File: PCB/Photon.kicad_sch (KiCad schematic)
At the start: 45 parts, among them J1 USB_C_Receptacle_USB2.0_14P, J2 Conn_01x05_Socket, Q1 IRLML6402, Q2 IRLML6402, SW1 TS-1088-AR02016, U1 PY32F002AL15S6TU, U2 TP4056, U3 RT8059GJ5, U4 BCR421UW6-7, U5 DW01A, U6 FS8205A, U7 BCR421UW6-7

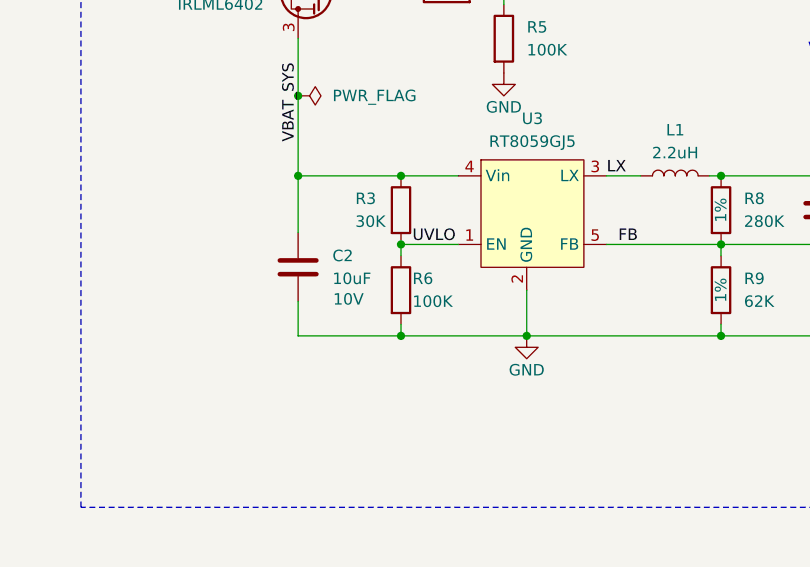
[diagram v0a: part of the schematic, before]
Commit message: updated debug header and changed resistors for UVLO
Applied teardrop to all vias. some were missing. Thickened trace from neg battery terminal. Updated gerbers
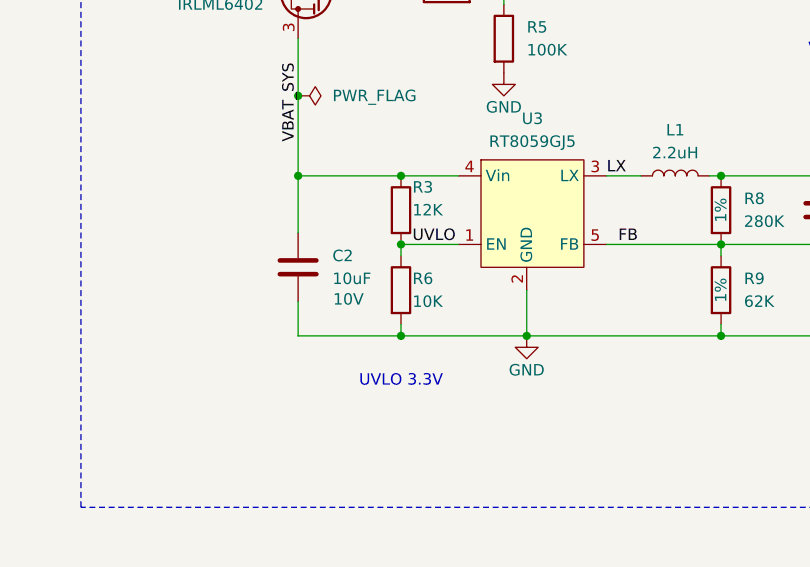
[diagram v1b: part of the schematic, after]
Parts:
- R3: value 30K -> 12K
- R6: value 100K -> 10K
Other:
- note added: "UVLO 3.3V"
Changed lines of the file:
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@@
 		)
 	)
+	(text "UVLO 3.3V\n"
+		(exclude_from_sim no)
+		(at 165.1 222.25 0)
+		(effects
+			(font
+				(size 1.27 1.27)
+			)
+		)
+	)
 	(text "If usb (5V) present \n-> disable buck"
 		(exclude_from_sim no)
@@
 			)
 		)
-		(property "Value" "100K"
+		(property "Value" "10K"
 			(at 166.37 213.36 0)
 			(effects
@@
 		(dnp no)
 		(property "Reference" "R3"
-			(at 160.02 201.93 0)
+			(at 166.37 200.66 0)
 			(effects
 				(font
@@
 			)
 		)
-		(property "Value" "30K"
-			(at 160.02 204.47 0)
+		(property "Value" "12K"
+			(at 166.37 203.2 0)
 			(effects
 				(font

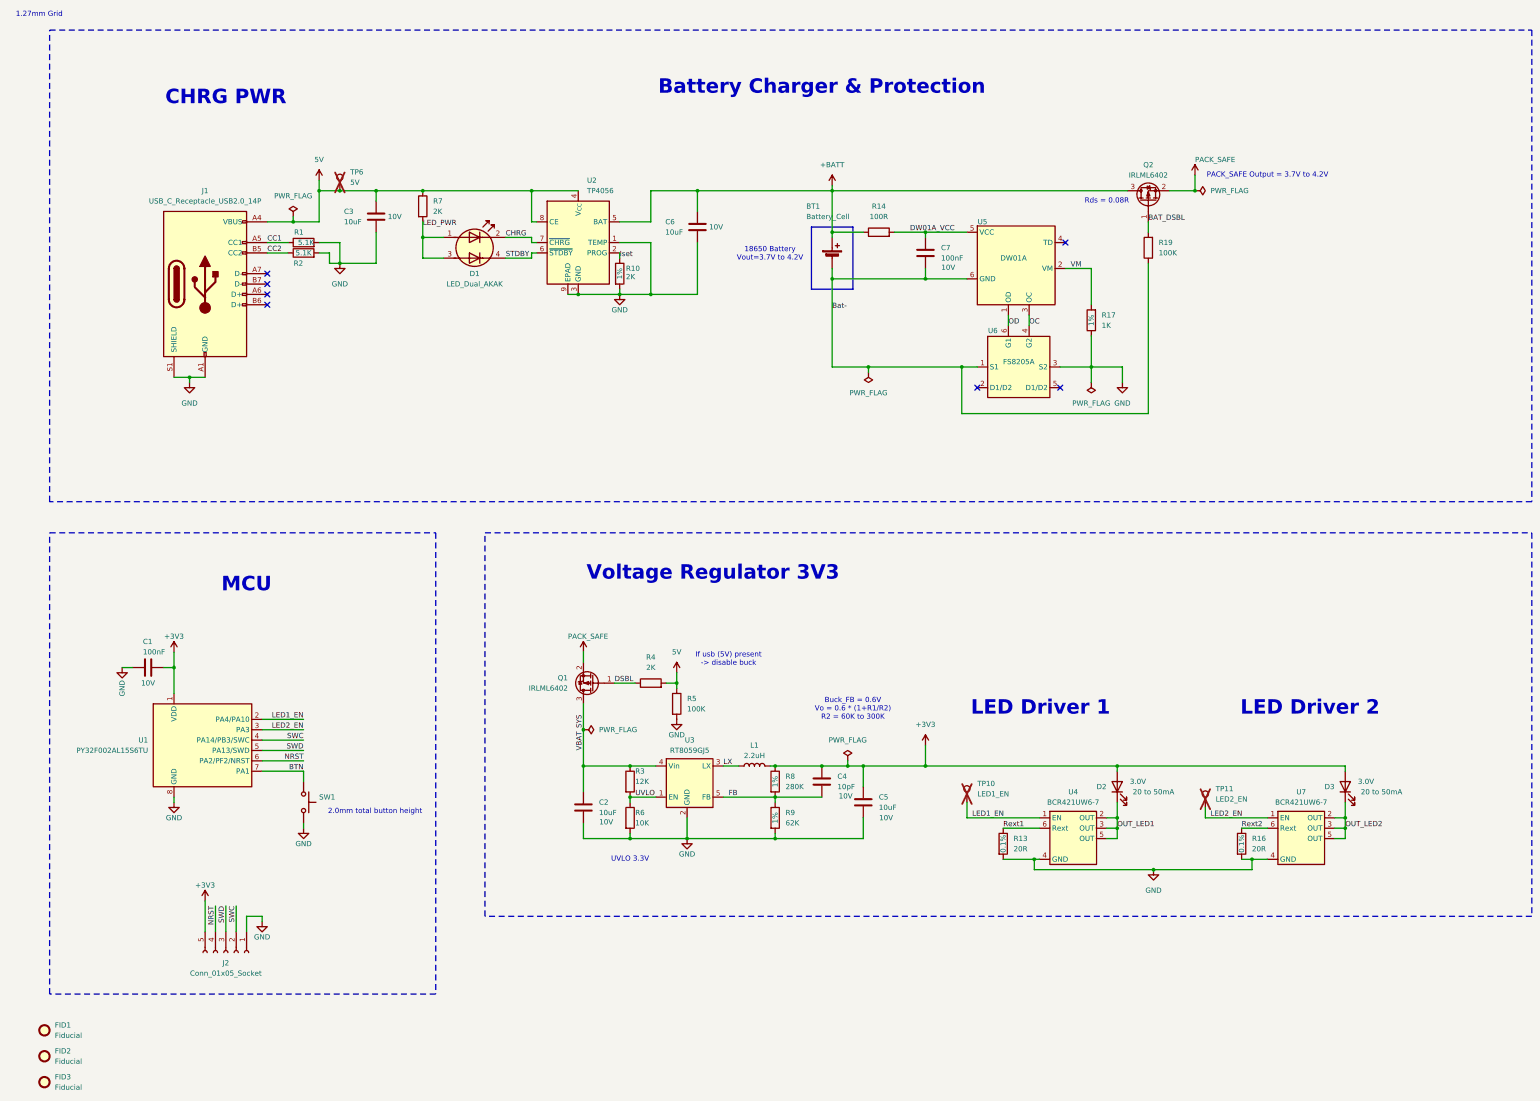
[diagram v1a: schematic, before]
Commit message: switch to smt32 mcu and cleaned up pcb
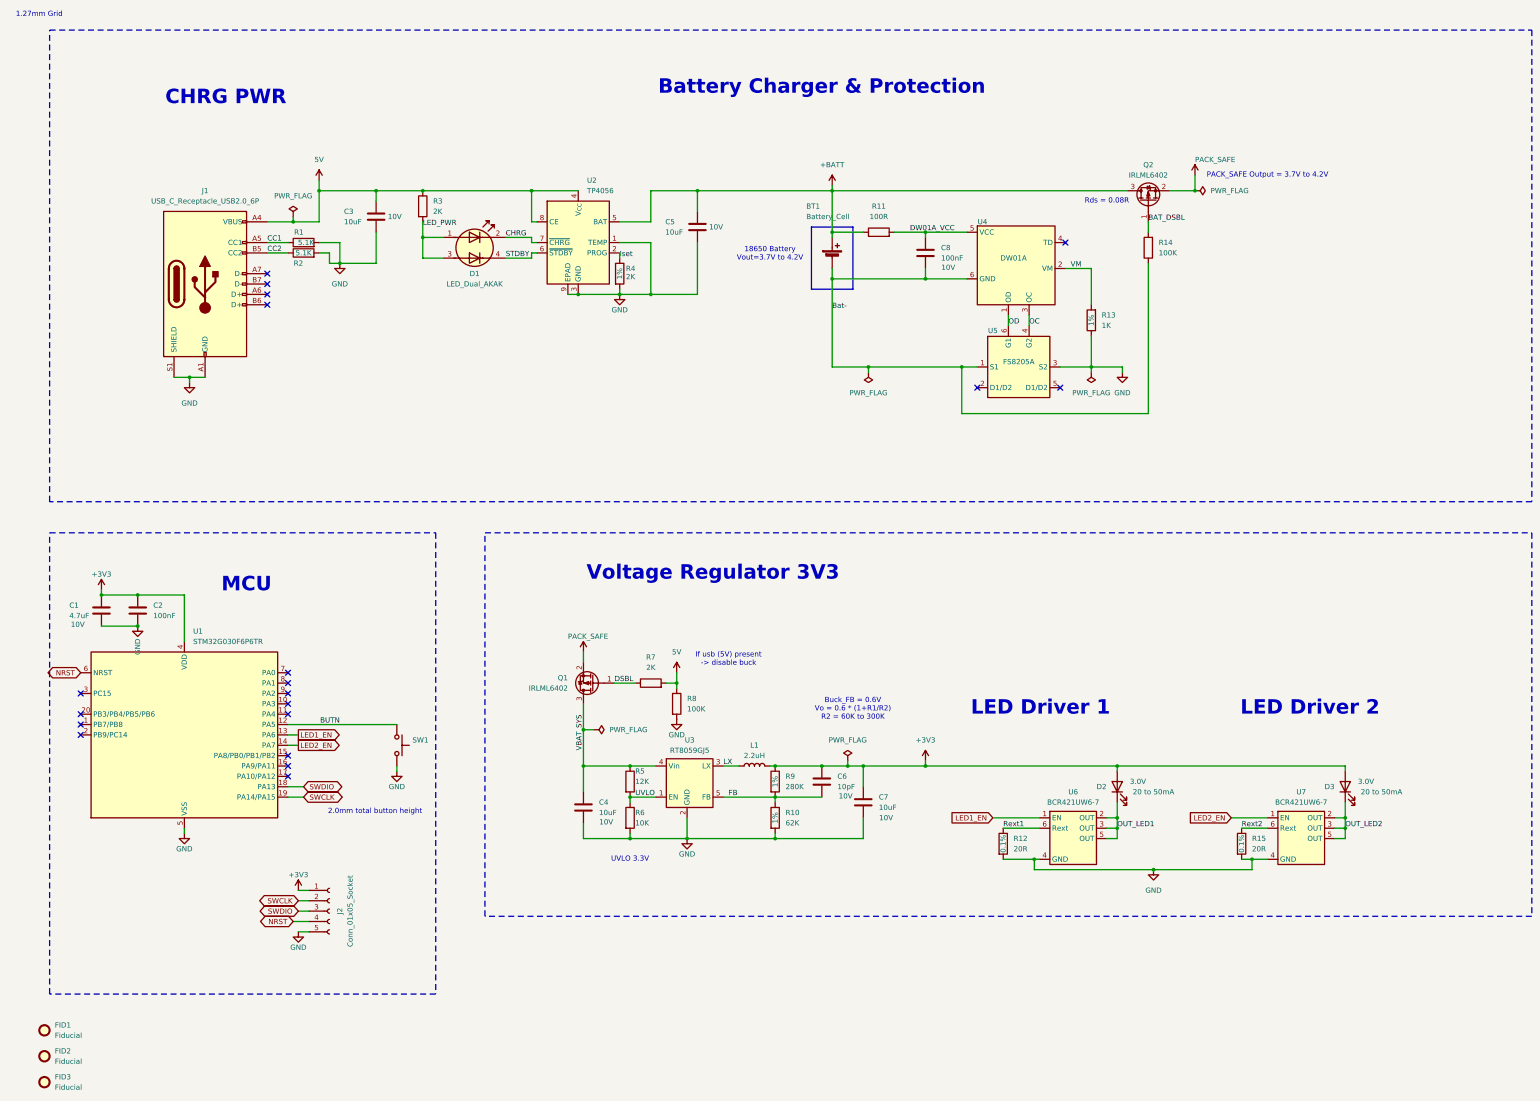
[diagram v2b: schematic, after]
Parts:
- removed TP10: LED1_EN, TestPoint:TestPoint_THTPad_D1.0mm_Drill0.5mm, symbol Connector:TestPoint
- removed TP11: LED2_EN, TestPoint:TestPoint_THTPad_D1.0mm_Drill0.5mm, symbol Connector:TestPoint
- removed TP6: 5V, TestPoint:TestPoint_THTPad_D1.0mm_Drill0.5mm, symbol Connector:TestPoint
- removed U1: PY32F002AL15S6TU, Package_SO:SOP-8_3.9x4.9mm_P1.27mm, symbol Photon:PY32F002AL15S6TU
- added C2: 100nF, Capacitor_SMD:C_0603_1608Metric, symbol Device:C
- added U1: STM32G030F6P6TR, Package_SO:TSSOP-20_4.4x6.5mm_P0.65mm, symbol MCU_ST_STM32G0:STM32G030F6Px
- C1: value 100nF -> 4.7uF; footprint Capacitor_SMD:C_0603_1608Metric -> Capacitor_SMD:C_0805_2012Metric
- J1: value USB_C_Receptacle_USB2.0_14P -> USB_C_Receptacle_USB2.0_6P
- renumbered C2 to C4, C6 to C5, C4 to C6, C5 to C7, C7 to C8, R9 to R10, R14 to R11, R13 to R12, R17 to R13, R19 to R14, R16 to R15, R7 to R3, R10 to R4, R3 to R5, R4 to R7, R5 to R8, R8 to R9, U5 to U4, U6 to U5, U4 to U6
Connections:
- net +3V3: now also J2.1 (Pin_1), C2.1, U1.4 (VDD); no longer J2.5 (Pin_5)
- net GND: now also J2.5 (Pin_5), C2.2, U1.5 (VSS); no longer J2.1 (Pin_1)
- net LED1_EN: now also U1.13 (PA6)
- net LED2_EN: now also U1.14 (PA7)
- net NRST: now also U1.6 (NRST)
- net BTN renamed BUTN
- net BUTN: now also U1.12 (PA5)
- net SWC renamed SWCLK
- net SWCLK: now also U1.19 (PA14/PA15)
- net SWD renamed SWDIO
- net SWDIO: now also U1.18 (PA13)
- no-connect marks 7 -> 19
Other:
- moved on the sheet: J2, SW1

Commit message: Schematic, Board and Firmware changes
Moved pins for LEDs onto timer channel capable pins to allow for future implementation if desired

Added 100nF cap to NRST pin

Changed programming footprint to use soic8 programmers found on Github

Changed buck to diodes fixed version (AP63203WU) for fewer components

Created Gerbers

Updated .ioc for pinout using timer channels and naming pins to match

Added footprint for debugger
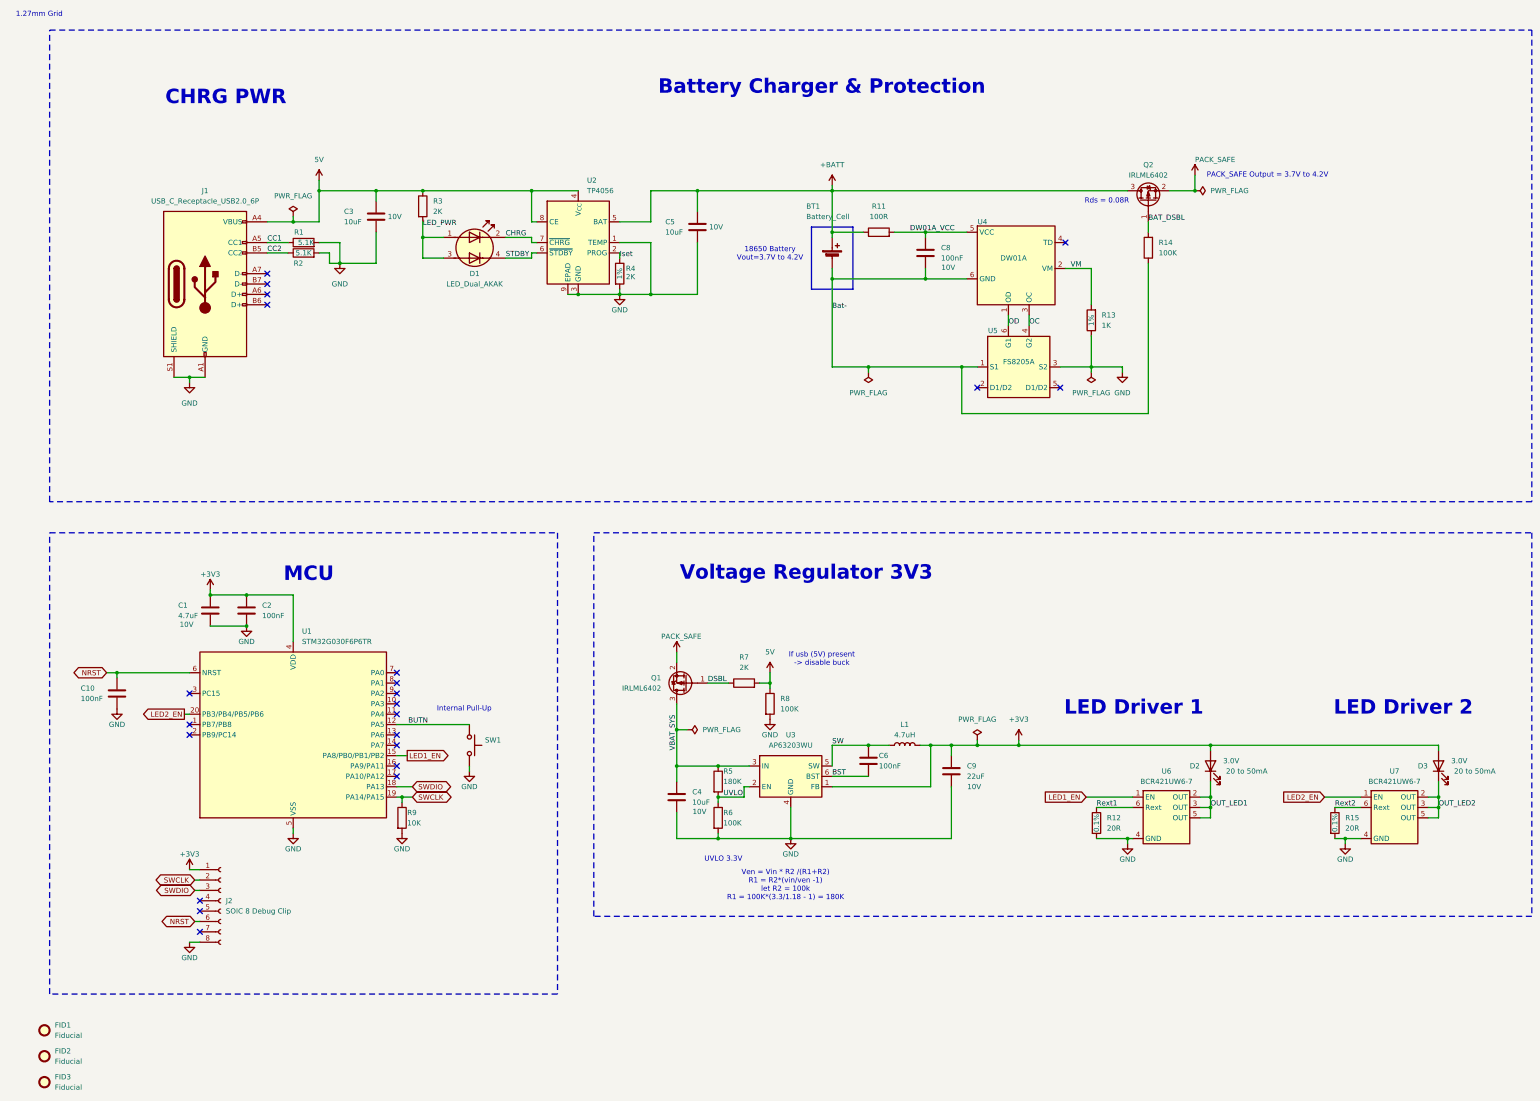
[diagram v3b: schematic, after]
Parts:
- removed C7: 10uF, Capacitor_SMD:C_0603_1608Metric, symbol Device:C
- removed J2: Conn_01x05_Socket, Connector_PinHeader_2.54mm:PinHeader_1x05_P2.54mm_Vertical, symbol Connector:Conn_01x05_Socket
- removed R10: 62K, Resistor_SMD:R_0603_1608Metric, symbol Device:R
- removed U3: RT8059GJ5, Package_TO_SOT_SMD:SOT-23-5, symbol Photon:RT8059GJ5
- added C10: 100nF, Capacitor_SMD:C_0603_1608Metric, symbol Device:C
- added C9: 22uF, Capacitor_SMD:C_0603_1608Metric, symbol Device:C
- added J2: SOIC 8 Debug Clip, SOIC Debug 8 ConN:SOIC_clipProgSmall, symbol Connector:Conn_01x08_Socket
- added U3: AP63203WU, Package_TO_SOT_SMD:TSOT-23-6, symbol Regulator_Switching:AP63203WU
- C6: value 10pF -> 100nF; Voltage 10V -> (none)
- L1: value 2.2uH -> 4.7uH
- R5: value 12K -> 180K
- R6: value 10K -> 100K
- R9: value 280K -> 10K; Tolerance 1% -> (none)
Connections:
- net LX is gone; now on net SW: L1.1
- net +3V3: now also C9.2, J2.1 (Pin_1), U3.1 (FB); no longer C6.2, R9.1
- net GND: now also R9.2, C10.1, C9.1, J2.8 (Pin_8), U3.4 (GND)
- net LED1_EN: now also U1.15 (PA8/PB0/PB1/PB2); no longer U1.13 (PA6)
- net LED2_EN: now also U1.20 (PB3/PB4/PB5/PB6); no longer U1.14 (PA7)
- net NRST: now also C10.2, J2.6 (Pin_6)
- net SWCLK: now also R9.1, J2.2 (Pin_2)
- net SWDIO: now also J2.3 (Pin_3)
- net UVLO: now also U3.2 (EN)
- net VBAT_SYS: now also U3.3 (IN)
- net FB renamed SW
- net SW: now also U3.5 (SW); no longer R9.2
- new net BST: C6.2, U3.6 (BST)
- no-connect marks 19 -> 22
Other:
- note added: "Internal Pull-Up"
- note added: "Ven = Vin * R2 /(R1+R2) R1 = R2*(vin/ven -1) let R2 = 100k R1 = 100K*(3.3/1.18 - 1) = 180K"
- note removed: "2.0mm total button height"
- note removed: "Buck_FB = 0.6V Vo = 0.6 * (1+R1/R2) R2 = 60K to 300K"
- moved on the sheet: C1, C2, C4, D2, D3, L1, Q1, R12, R15, R5, R6, R7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

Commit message: added new inductor links
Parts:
- L1: Part# (none) -> ANR3015T4R7M; Supplier https://jlcpcb.com/partdetail/SXN_Shun_Xiang_Nuo_Elec-SM352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 -> https://www.lcsc.com/product-detail/C7427089.html?s_z=n_4.7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
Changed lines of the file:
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@@
 			)
 		)
-		(property "Datasheet" "https://jlcpcb.com/api/file/downloadByFileSystemAccessId/8588935238940966912"
+		(property "Datasheet" "https://www.lcsc.com/datasheet/C7427089.pdf"
 			(at 232.41 194.31 0)
 			(effects
@@
 			)
 		)
-		(property "Supplier" "https://jlcpcb.com/partdetail/SXN_Shun_Xiang_Nuo_Elec-SM35212R2MT/C9890"
+		(property "Supplier" "https://www.lcsc.com/product-detail/C7427089.html?s_z=n_4.7uh"
 			(at 232.41 194.31 90)
 			(effects
+				(font
+					(size 1.27 1.27)
+				)
+				(hide yes)
+			)
+		)
+		(property "Part#" "ANR3015T4R7M"
+			(at 232.41 194.31 90)
+			(effects

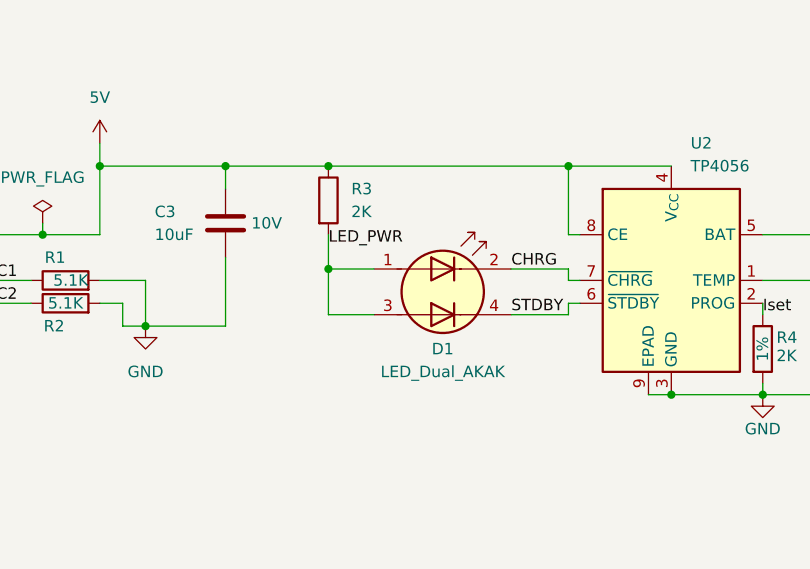
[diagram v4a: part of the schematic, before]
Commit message: Component changes for better button and LED
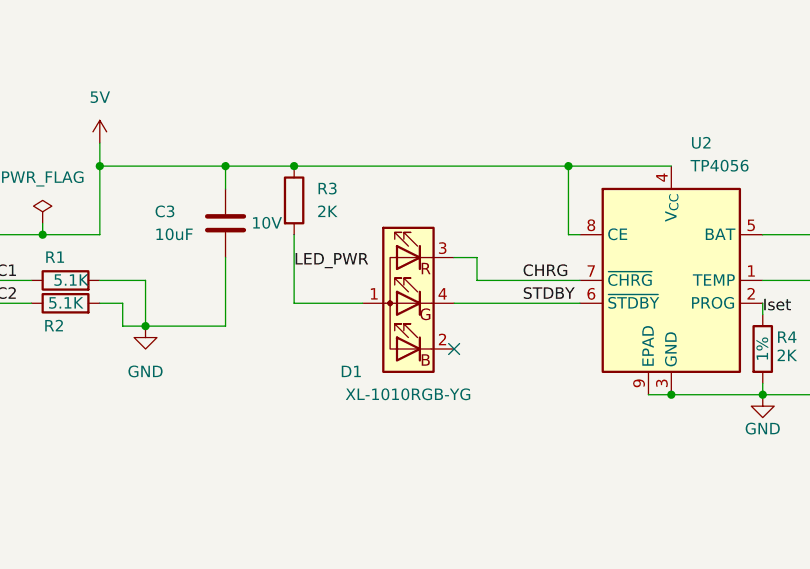
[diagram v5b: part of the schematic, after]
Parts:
- BT1: footprint Photon:Spring Battery TH -> Photon:18650 Tin Strips
- D1: value LED_Dual_AKAK -> XL-1010RGB-YG; footprint Photon:3.9mm Bi directional side mount LED -> LED_SMD:LED_Wurth_150044M155260; symbol Device:LED_Dual_AKAK -> Device:LED_ABRG; Supplier https://www.lcsc.com/product-detail/C965883.html -> https://www.lcsc.com/product-detail/C965834.html?spm=wm.fly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
- SW1: footprint Photon:5mm Push Button -> Button_Switch_SMD:SW_Push_1P1T_XKB_TS-1187A
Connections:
- net CHRG: now also D1.3 (RK); no longer D1.2 (K1)
- net LED_PWR: no longer D1.3 (A2)
- no-connect marks 22 -> 23
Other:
- moved on the sheet: R3
